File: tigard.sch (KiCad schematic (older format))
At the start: 17 parts, among them J1 USB_C_Receptacle_USB2.0, Q1 BSH103, SW1 SW_SP3T, SW2 SW_DPDT, U1 AP7365-18, U2 AP7365-33

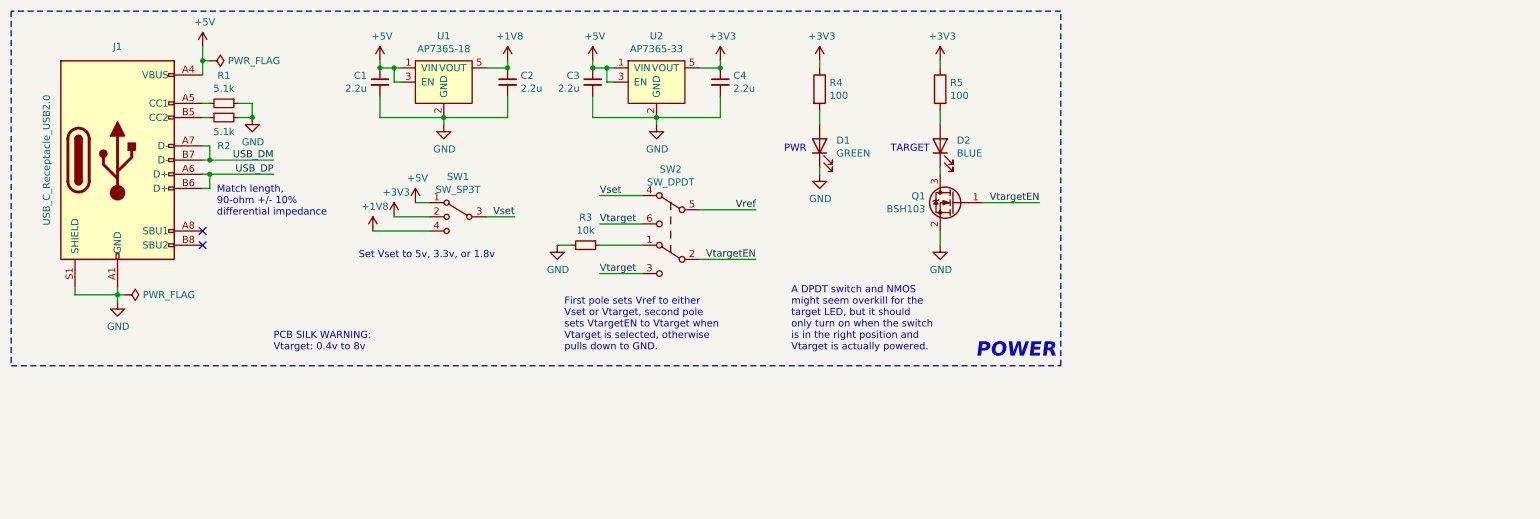
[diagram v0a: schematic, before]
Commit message: Add JTAG, UART, SPI, SWD, I2C connectors
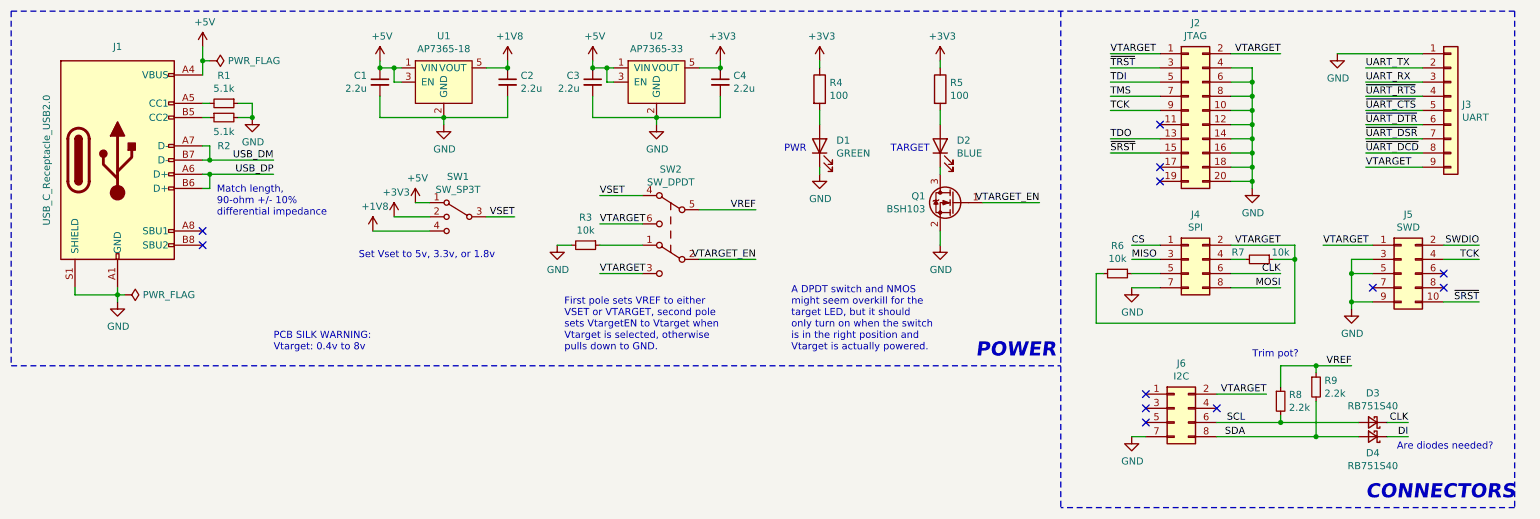
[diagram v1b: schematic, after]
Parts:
- added D3, D4: RB751S40, Diode_SMD:D_SOD-523, symbol Device:D_Schottky_Small
- added J2: JTAG, Connector_PinHeader_2.54mm:PinHeader_2x10_P2.54mm_Vertical, symbol Connector_Generic:Conn_02x10_Odd_Even
- added J3: UART, Connector_PinHeader_2.54mm:PinHeader_1x09_P2.54mm_Vertical, symbol Connector_Generic:Conn_01x09
- added J4: SPI, Connector_PinHeader_2.54mm:PinHeader_2x04_P2.54mm_Vertical, symbol Connector_Generic:Conn_02x04_Odd_Even
- added J5: SWD, Connector_PinHeader_1.27mm:PinHeader_2x05_P1.27mm_Vertical, symbol Connector_Generic:Conn_02x05_Odd_Even
- added J6: I2C, Connector_PinHeader_2.54mm:PinHeader_2x04_P2.54mm_Vertical, symbol Connector_Generic:Conn_02x04_Odd_Even
- added R6, R7: 10k, Resistor_SMD:R_0402_1005Metric, symbol Device:R_Small
- added R8, R9: 2.2k, Resistor_SMD:R_0402_1005Metric, symbol Device:R_Small
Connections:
- net GND: now also J2.10 (Pin_10), J2.12 (Pin_12), J2.14 (Pin_14), J2.16 (Pin_16), J2.18 (Pin_18), J2.20 (Pin_20), J2.4 (Pin_4), J2.6 (Pin_6), J2.8 (Pin_8), J3.1 (Pin_1), J4.7 (Pin_7), J5.3 (Pin_3), J5.5 (Pin_5), J5.9 (Pin_9), J6.7 (Pin_7)
- net Vref renamed VREF
- net VREF: now also R8.1, R9.1
- net Vset renamed VSET
- net Vtarget renamed VTARGET
- net VTARGET: now also J2.1 (Pin_1), J2.2 (Pin_2), J3.9 (Pin_9), J4.2 (Pin_2), J5.1 (Pin_1), J6.2 (Pin_2), R6.2, R7.1
- net VtargetEN renamed VTARGET_EN
- new net: J4.4 (Pin_4), R7.2
- new net: J4.5 (Pin_5), R6.1
- new net CLK: D3.1 (K), J4.6 (Pin_6)
- new net CS: J4.1 (Pin_1)
- new net DI: D4.1 (K)
- new net MISO: J4.3 (Pin_3)
- new net MOSI: J4.8 (Pin_8)
- new net SCL: D3.2 (A), J6.6 (Pin_6), R8.2
- new net SDA: D4.2 (A), J6.8 (Pin_8), R9.2
- new net SWDIO: J5.2 (Pin_2)
- new net TCK: J2.9 (Pin_9), J5.4 (Pin_4)
- new net TDI: J2.5 (Pin_5)
- new net TDO: J2.13 (Pin_13)
- new net TMS: J2.7 (Pin_7)
- new net UART_RX: J3.3 (Pin_3)
- new net UART_TX: J3.2 (Pin_2)
- new net ~SRST: J2.15 (Pin_15), J5.10 (Pin_10)
- new net ~TRST: J2.3 (Pin_3)
- new net ~UART_CTS: J3.5 (Pin_5)
- new net ~UART_DCD: J3.8 (Pin_8)
- new net ~UART_DSR: J3.7 (Pin_7)
- new net ~UART_DTR: J3.6 (Pin_6)
- new net ~UART_RTS: J3.4 (Pin_4)
- no-connect marks 2 -> 12
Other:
- note added: "Are diodes needed?"
- note added: "CONNECTORS"
- note added: "First pole sets VREF to either\nVSET or VTARGET, second pole\nsets VtargetEN to Vtarget when\nVtarget is selected, otherwise\npulls down to GND."
- note added: "Trim pot?"
- note removed: "First pole sets Vref to either\nVset or Vtarget, second pole\nsets VtargetEN to Vtarget when\nVtarget is selected, otherwise\npulls down to GND."

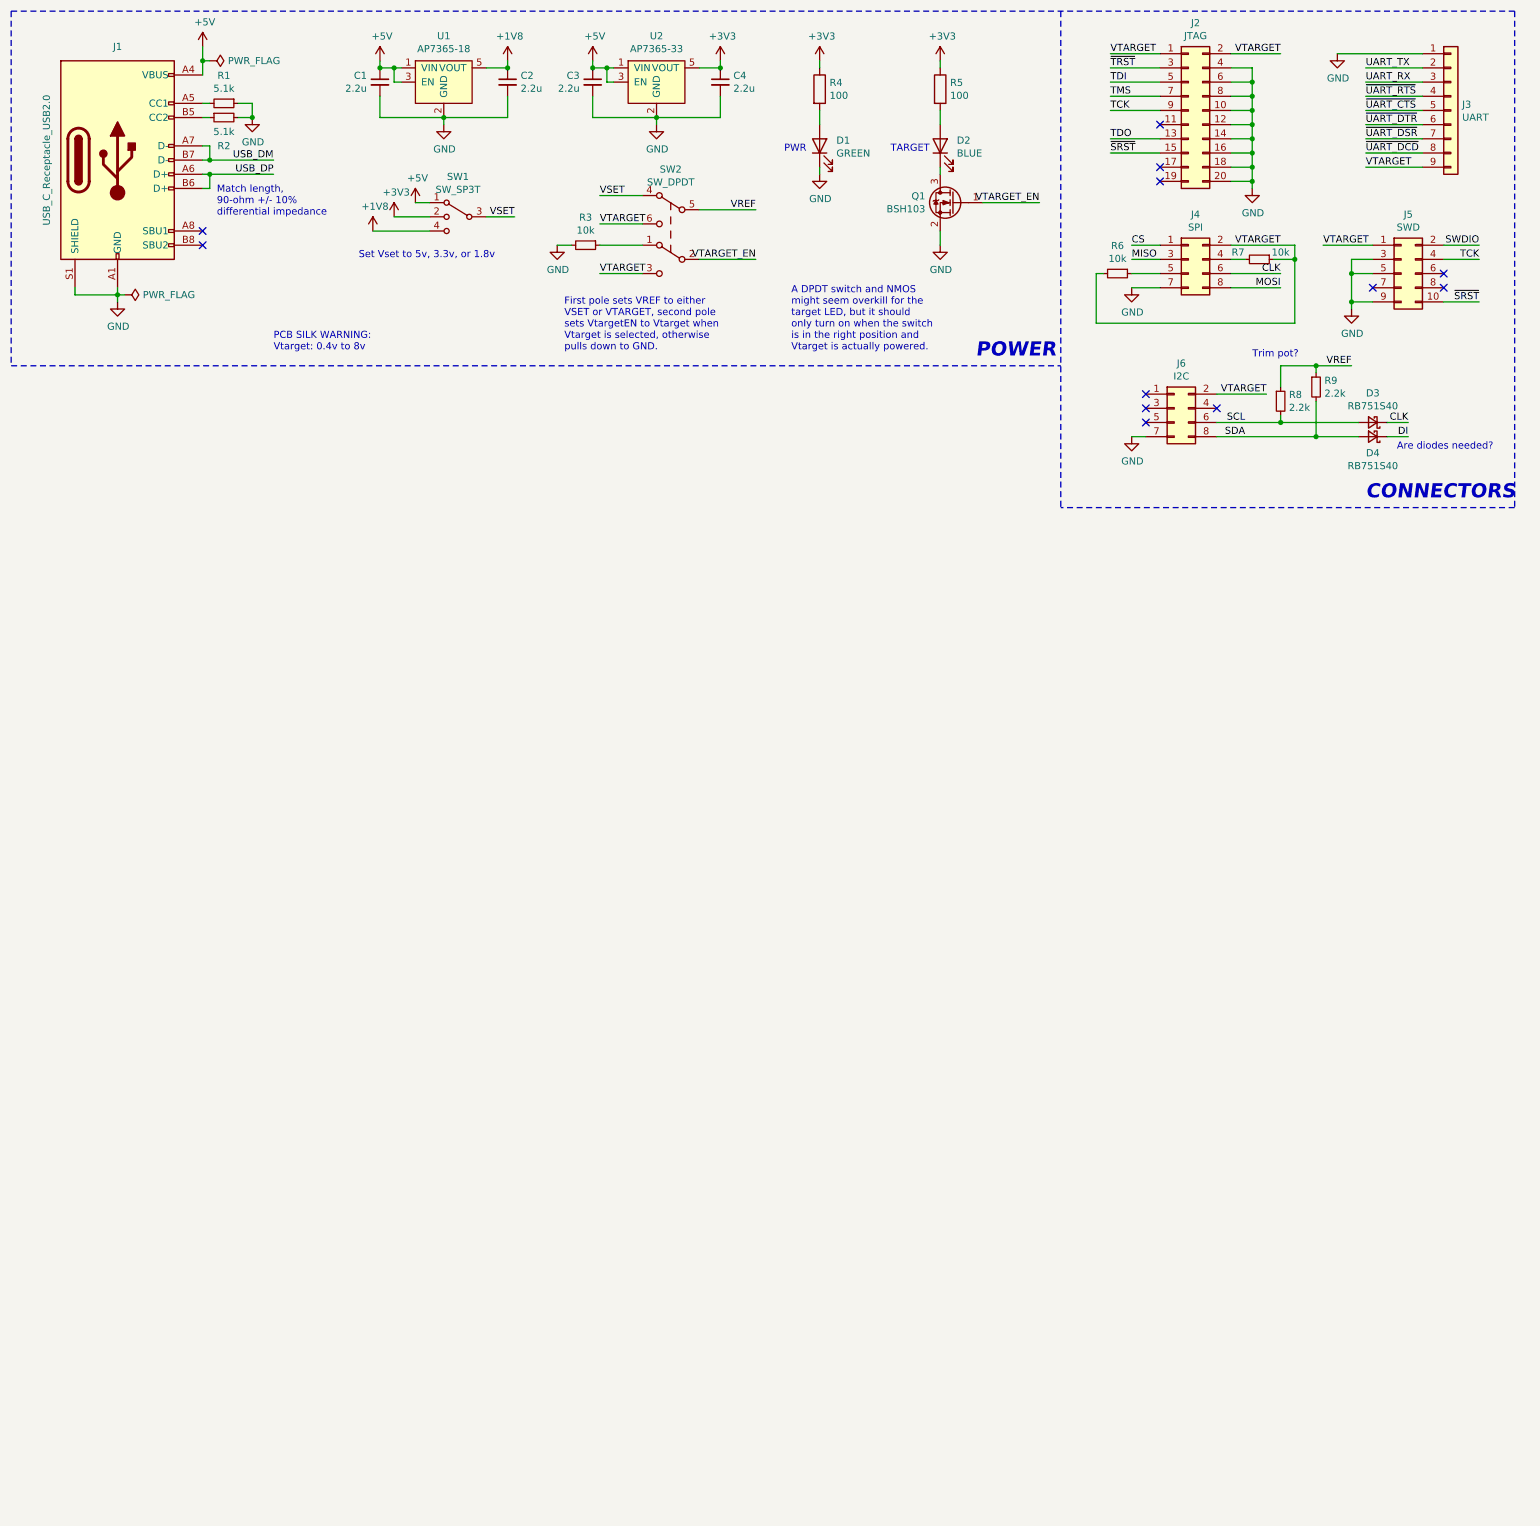
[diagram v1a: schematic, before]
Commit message: Add FT2232H and EEPROM to schematic
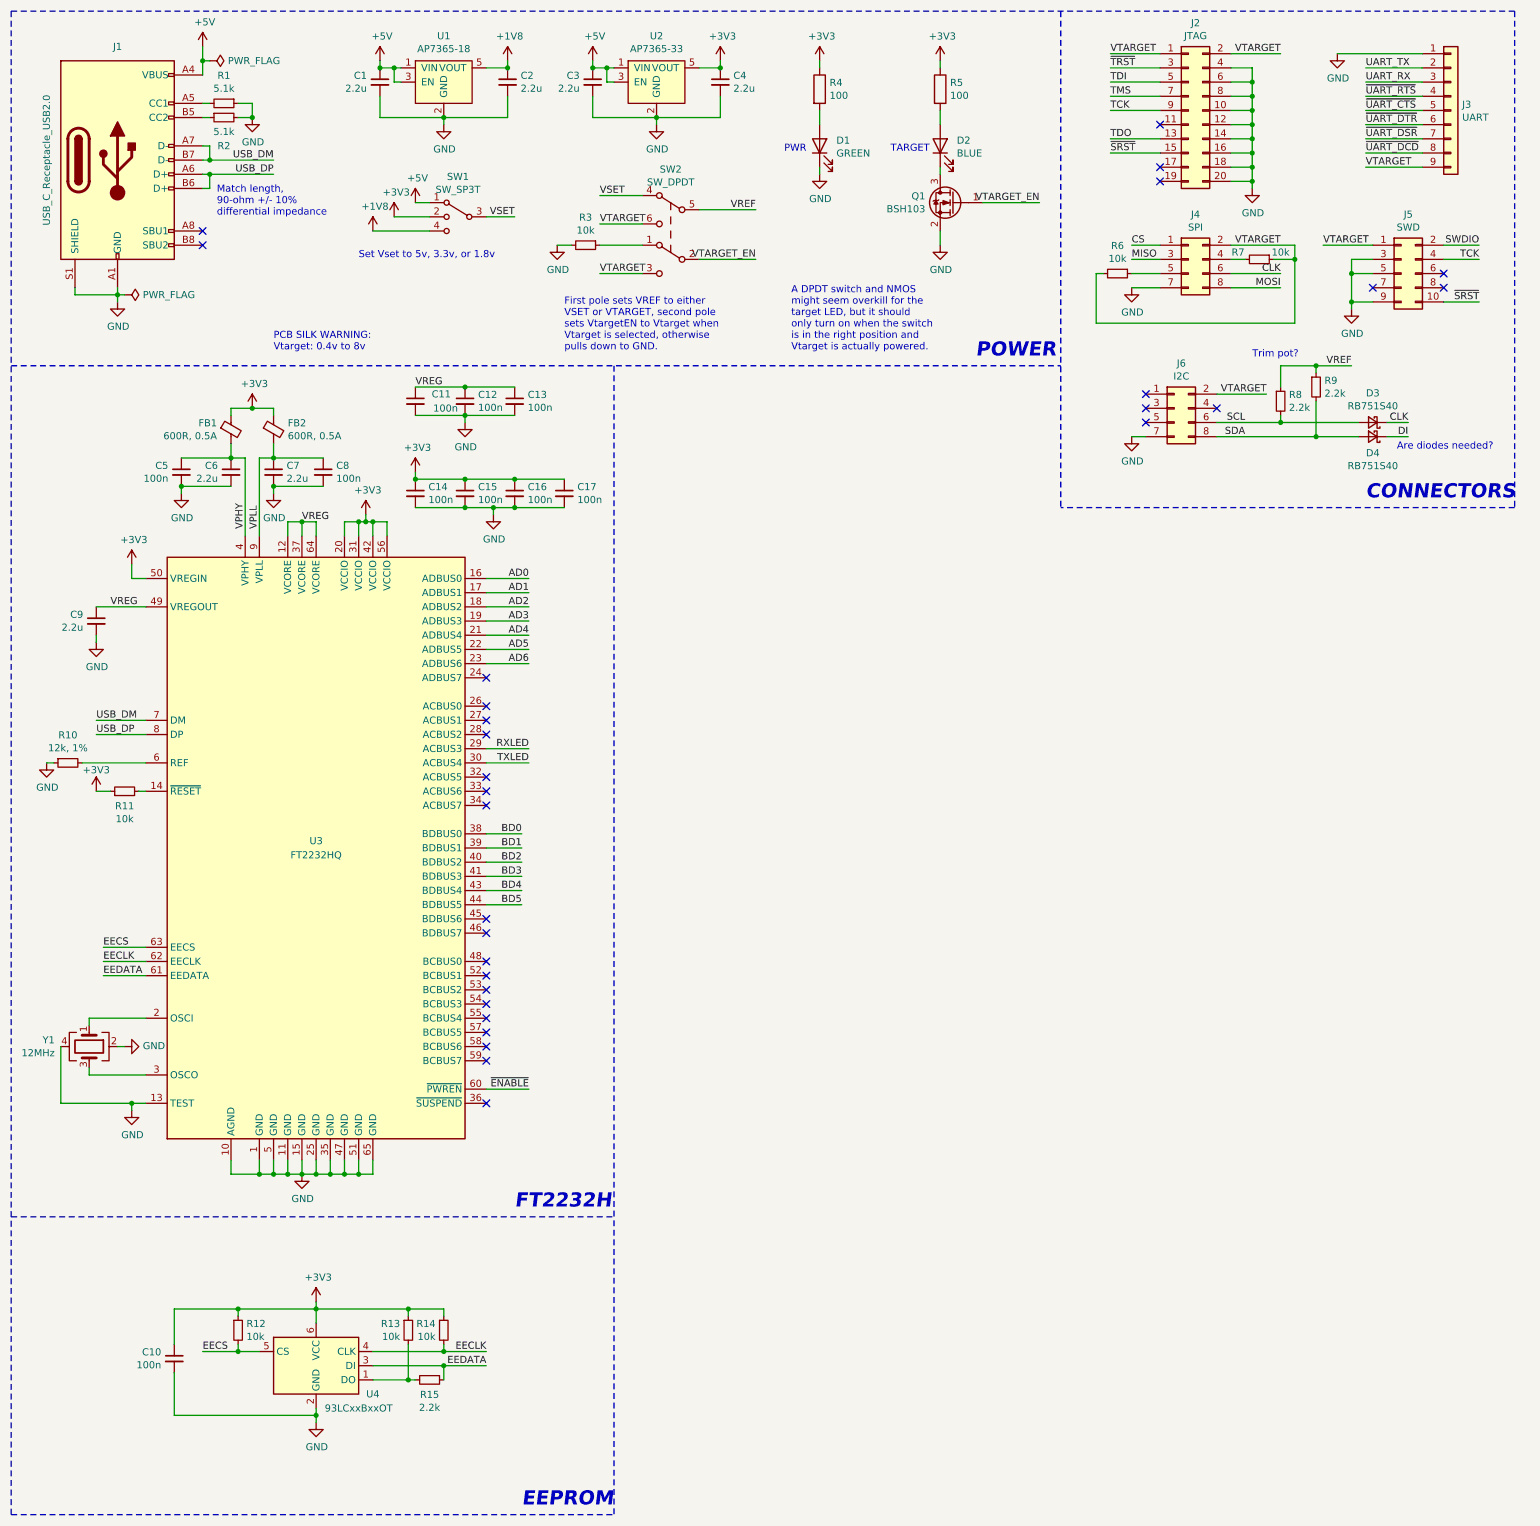
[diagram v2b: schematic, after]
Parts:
- added C10, C11, C12, C13, C14, C15, C16, C17, C5, C8: 100n, Capacitor_SMD:C_0402_1005Metric, symbol Device:C_Small
- added C6, C7, C9: 2.2u, Capacitor_SMD:C_0603_1608Metric, symbol Device:C_Small
- added FB1, FB2: 600R, 0.5A, Inductor_SMD:L_0402_1005Metric, symbol Device:Ferrite_Bead_Small
- added R10: 12k, 1%, Resistor_SMD:R_0402_1005Metric, symbol Device:R_Small
- added R11, R12, R13, R14: 10k, Resistor_SMD:R_0402_1005Metric, symbol Device:R_Small
- added R15: 2.2k, Resistor_SMD:R_0402_1005Metric, symbol Device:R_Small
- added U3: FT2232HQ, Package_DFN_QFN:QFN-64-1EP_9x9mm_P0.5mm_EP4.35x4.35mm, symbol Interface_USB:FT2232HQ
- added U4: 93LCxxBxxOT, Package_TO_SOT_SMD:SOT-23-6, symbol Memory_EEPROM:93LCxxBxxOT
- added Y1: 12MHz, Crystal:Crystal_SMD_3225-4Pin_3.2x2.5mm, symbol Device:Crystal_GND24
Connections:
- net +3V3: now also C10.1, C14.1, C15.1, C16.1, C17.1, FB1.1, FB2.1, R11.1, R12.1, R13.1, R14.1, U3.20 (VCCIO), U3.31 (VCCIO), U3.42 (VCCIO), U3.50 (VREGIN), U3.56 (VCCIO), U4.6 (VCC)
- net GND: now also C10.2, C11.2, C12.2, C13.2, C14.2, C15.2, C16.2, C17.2, C5.2, C6.2, C7.2, C8.2, C9.2, R10.1, U3.1 (GND), U3.10 (AGND), U3.11 (GND), U3.13 (TEST), U3.15 (GND), U3.25 (GND), U3.35 (GND), U3.47 (GND), U3.5 (GND), U3.51 (GND), U3.65 (GND), U4.2 (GND), Y1.2, Y1.4
- net USB_DM: now also U3.7 (DM)
- net USB_DP: now also U3.8 (DP)
- new net: R11.2, U3.14 (~RESET)
- new net: U3.2 (OSCI), Y1.1
- new net: U3.3 (OSCO), Y1.3
- new net: R10.2, U3.6 (REF)
- new net: R13.2, R15.2, U4.1 (DO)
- new net AD0: U3.16 (ADBUS0)
- new net AD1: U3.17 (ADBUS1)
- new net AD2: U3.18 (ADBUS2)
- new net AD3: U3.19 (ADBUS3)
- new net AD4: U3.21 (ADBUS4)
- new net AD5: U3.22 (ADBUS5)
- new net AD6: U3.23 (ADBUS6)
- new net BD0: U3.38 (BDBUS0)
- new net BD1: U3.39 (BDBUS1)
- new net BD2: U3.40 (BDBUS2)
- new net BD3: U3.41 (BDBUS3)
- new net BD4: U3.43 (BDBUS4)
- new net BD5: U3.44 (BDBUS5)
- new net EECLK: R14.2, U3.62 (EECLK), U4.4 (CLK)
- new net EECS: R12.2, U3.63 (EECS), U4.5 (CS)
- new net EEDATA: R15.1, U3.61 (EEDATA), U4.3 (DI)
- new net RXLED: U3.29 (ACBUS3)
- new net TXLED: U3.30 (ACBUS4)
- new net VPHY: C5.1, C6.1, FB1.2, U3.4 (VPHY)
- new net VPLL: C7.1, C8.1, FB2.2, U3.9 (VPLL)
- new net VREG: C11.1, C12.1, C13.1, C9.1, U3.12 (VCORE), U3.37 (VCORE), U3.49 (VREGOUT), U3.64 (VCORE)
- new net ~ENABLE: U3.60 (~PWREN)
- no-connect marks 12 -> 30
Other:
- note added: "EEPROM"
- note added: "FT2232H"
